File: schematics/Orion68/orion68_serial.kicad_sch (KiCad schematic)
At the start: 32 parts, among them J700 Euro96pin, J701 RS232_1, J702 RS232_1, J703 RS232_1, U18_C? 100nf, U19 74HC138, U20 74HC138, U23 74LS139, U701 UART1, U702 UART2, U703 UART3, Y1 14.745600

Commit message: updating
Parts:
- added U27: 74LS32, symbol 74xx:74LS32
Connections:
- net +5V: no longer U20.6 (E2)
- net A10: no longer U20.3 (A2)
- net A11: now also U27.2; no longer U20.4 (~{E0})
- net A8: no longer U20.1 (A0)
- net A9: no longer U20.2 (A1)
- net /AS: now also U27.5
- net /IO_CS: now also J700.84, U27.12; no longer J700.85, U20.5 (~{E1})
- net /LDS: now also U27.1
- net /UART_CS: now reaches J700.83
- new net: U20.4 (~{E0}), U27.8
- new net: U20.5 (~{E1}), U27.11
- new net: U27.3, U27.9
- new net: U27.10, U27.6
- new net A12: U20.1 (A0)
- new net A13: U20.2 (A1)
- new net A14: U20.3 (A2)
- new net A15: U20.6 (E2)
- new net /IO_CS1: U27.13
- new net /MEM_CS: J700.85
- new net /cpuwr: U27.4
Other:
- note added: "FF9000 – FF9FFF UART0 FF9000 – FF9FFF UART1 FF9900 – FF9FFF UART2 FF9000 – FF9FFF UART3"
- note removed: "FF0100 – FF00FF UART0 FF0200 – FF01FF UART1 FF0300 – FF02FF UART2 FF0400 – FF03FF UART3"
- moved on the sheet: U20

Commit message: B column DIN conn. all in GND
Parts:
- removed J700: Euro96pin, ConnPdSilva:conn_euro96, symbol ConnPdSilva:ConnEuro96
- removed U19: 74HC138, symbol 74xx:74HC138
- removed U23: 74LS139, symbol 74xx:74LS139
- removed U27: 74LS32, symbol 74xx:74LS32
- added J700 (x2): Euro96pin, ConnPdSilva:conn_euro96, symbol ConnPdSilva:ConnEuro96
- added U28: ~, symbol pdSilva:74HC4078
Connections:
- net +12V: now also J700.92, J700.92
- net +5V: now also J700.1, J700.1, J700.33, J700.33, J700.65, J700.65, U28.14 (VCC)
- net -5V: now also J700.94, J700.94
- net A10: now also U20.3 (A2)
- net A11: now also U20.4 (~{E0})
- net A12: now also U28.2 (I1); no longer U20.1 (A0)
- net A13: now also U28.3 (I2); no longer U20.2 (A1)
- net A14: now also U20.6 (E2); no longer U20.3 (A2)
- net A15: now also U28.4 (I3); no longer U20.6 (E2)
- net A8: now also U20.1 (A0)
- net A9: now also U20.2 (A1)
- net ALE: now also J700.73
- net BA0: now also J700.18
- net BA1: now also J700.19, J700.19
- net BA10: now also J700.28, J700.28
- net BA11: now also J700.29, J700.29
- net BA12: now also J700.30, J700.30
- net BA13: now also J700.31, J700.31
- net BA14: now also J700.63, J700.91
- net BA15: now also J700.62, J700.90
- net BA16: now also J700.61, J700.89
- net BA17: now also J700.60, J700.88
- net BA18: now also J700.59, J700.87
- net BA19: now also J700.58, J700.86
- net BA2: now also J700.20, J700.20
- net BA20: now also J700.57, J700.81
- net BA21: now also J700.56, J700.80
- net BA22: now also J700.55, J700.79
- net BA23: now also J700.54, J700.78
- net BA3: now also J700.21, J700.21
- net BA4: now also J700.22, J700.22
- net BA5: now also J700.23, J700.23
- net BA6: now also J700.24, J700.24
- net BA7: now also J700.25, J700.25
- net BA8: now also J700.26, J700.26
- net BA9: now also J700.27, J700.27
- net BD0: now also J700.2, J700.2
- net BD1: now also J700.3, J700.3
- net BD10: now also J700.12, J700.12
- net BD11: now also J700.13, J700.13
- net BD12: now also J700.14, J700.14
- net BD13: now also J700.15, J700.15
- net BD14: now also J700.16, J700.16
- net BD15: now also J700.17, J700.17
- net BD2: now also J700.4, J700.4
- net BD3: now also J700.5, J700.5
- net BD4: now also J700.6, J700.6
- net BD5: now also J700.7, J700.7
- net BD6: now also J700.8, J700.8
- net BD7: now also J700.9, J700.9
- net BD8: now also J700.10, J700.10
- net BD9: now also J700.11, J700.11
- net BOOTIN: now also J700.87
- net B/AS: now also J700.43, J700.69
- net B/LDS: now also J700.70, J700.70
- net B/UDS: now also J700.71, J700.71
- net CPU_CLK: now also J700.81
- net CRUCLK: now also J700.35
- net CRUIN: now also J700.36
- net CRUOUT: now also J700.37
- net DBIN: now also J700.38
- net DT/R: now also J700.75
- net E: now also J700.34
- net GND: now also J700.32, J700.32, J700.64, J700.64, J700.93, J700.93, J700.95, J700.95, J700.96, J700.96
- net GNDREF: now also U28.10 (I6), U28.7 (VCC), U28.9 (I5)
- net HLDA: now also J700.52
- net IAQ: now also J700.39
- net IRQ2: now also J700.48
- net IRQ3: now also J700.49
- net IRQ4: now also J700.50
- net IRQ5: now also J700.89
- net IRQ6: now also J700.90
- net IRQ7: now also J700.91
- net M/IO: now also J700.76
- net NMI: now also J700.41
- net PWR_GOOD: now also J700.88
- net RESET: now also J700.67, J700.67
- net Res9: now also J700.69
- net TICK_IN: now also J700.86
- net /AS: now also U28.5 (I4)
- net /BERR: now also J700.68
- net /CSA: now also U20.15 (~{Y0}); no longer U20.14 (~{Y1})
- net /CSB: now also U20.14 (~{Y1}); no longer U20.13 (~{Y2})
- net /CSC: now also U20.13 (~{Y2}); no longer U20.12 (~{Y3})
- net /CSD: now also U20.12 (~{Y3}); no longer U20.11 (~{Y4})
- net /DEN: now also J700.74
- net /HALT: now also J700.53
- net /HOLD: now also J700.42
- net /INTA: now also J700.72
- net /INTR: now also J700.40
- net /IO_CS: now also J700.84, J700.84, U28.11 (I7)
- net /IO_CS1: now also J700.82, J700.82, U28.12 (I8)
- net /M1: now also J700.79
- net /MEM_CS: now also J700.85, J700.85
- net /RESET: now also J700.66, J700.66
- net /RFSH: now also J700.80
- net /RST: now also J700.51
- net /SSO: now also J700.77
- net /UART_CS: now also J700.83
- net /WAIT: now also J700.78
- net /iord: now also J700.44
- net /iowr: now also J700.47
- net /memrd: now also J700.45
- net /memwr: now also J700.46
- net at U20.5 (~{E1}): now also U28.1 (O1)
- no-connect marks 24 -> 20
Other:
- note added: "1 2 3 4 5 6 7 8 9 10 11 12 13 14 15"
- note added: "15 14 13 12 11 10"
- note added: "15 14 13 12 11 10 9 8 7 6 5 4 3 2 1"
- note added: "23 22 21 20 19 18 17 16 15 14 13 12 11 10 09 08 07 06 05 04 03 02 01 00 1 1 1 1 1 1 1 1 0 1 0 0 0 0 0 0 0 0 0 0 0 0 0 0 F F 4 0 0 0"
- note added: "FF4000 – FF40FF UART0 FF4100 – FF91FF UART1 FF4200 - FF92FF UART2 FF4300 - FF93FF UART3"
- note removed: "FF9000 – FF9FFF UART0 FF9000 – FF9FFF UART1 FF9900 – FF9FFF UART2 FF9000 – FF9FFF UART3"
- note removed: "O que o manual está te dizendo (Tradução para o Orion68K): GINT (Global Interrupt) no Pino INT0: Se você configurar o bit AFR[4] como '1', o chip para de usar vários pinos de interrupção e concentra tudo no pino INT0. Isso é ótimo para economizar trilhas no seu wire-up. Inversão via Software (O melhor de tudo!): O bit AFR[5] é o seu "inversor digital". Se você deixar AFR[5] em '0' (que é o padrão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"
- moved on the sheet: U20

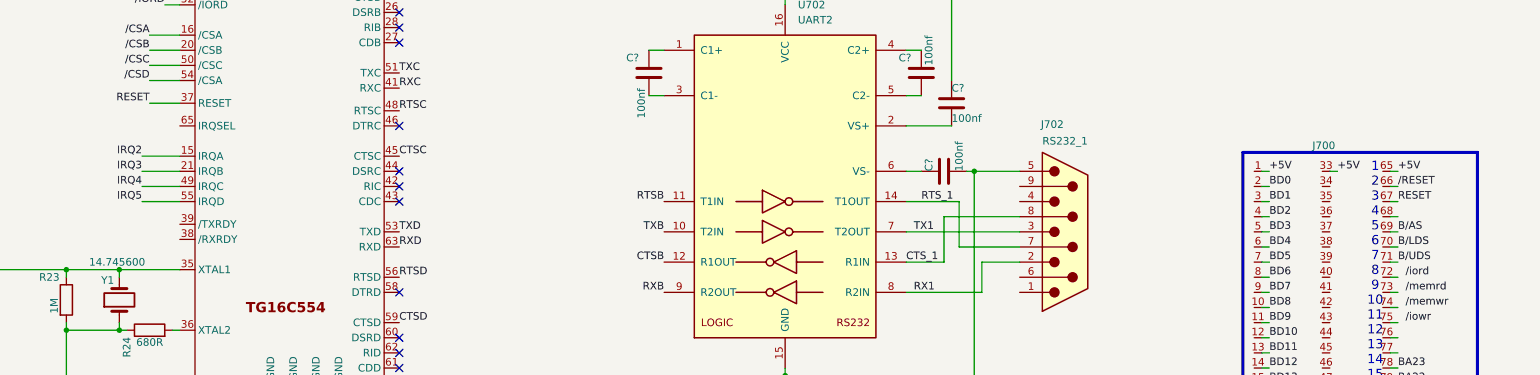
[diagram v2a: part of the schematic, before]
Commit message: Added drv_keboard
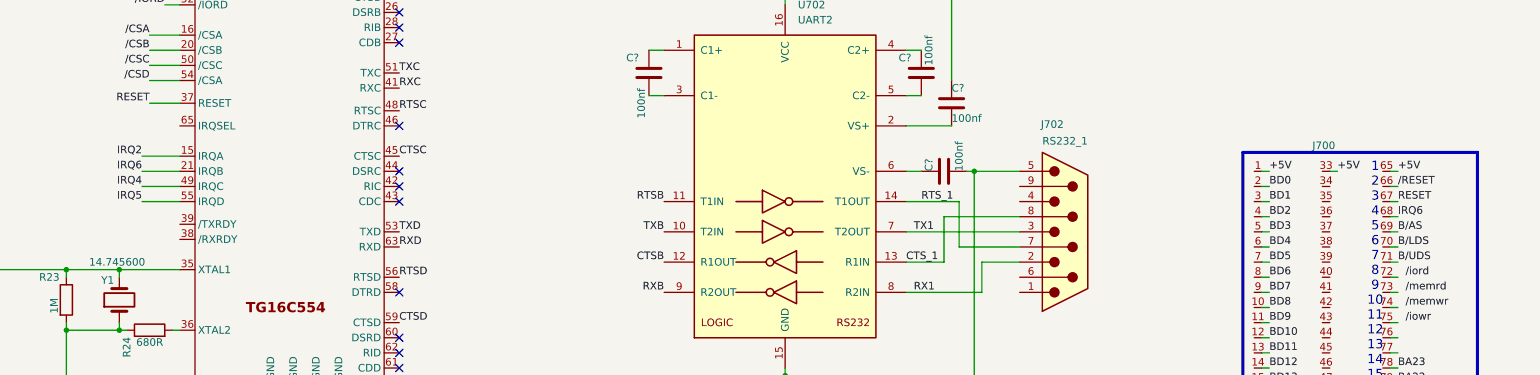
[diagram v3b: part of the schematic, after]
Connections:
- net IRQ3: no longer U700.21 (IRQB)
- net IRQ6: now also J700.68, U700.21 (IRQB)
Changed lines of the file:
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@@
+		)
+	)
+	(label "IRQ6"
+		(at 361.95 142.24 0)
+		(effects
+			(font
+				(size 1.27 1.27)
+			)
+			(justify left bottom)
 		)
 	)
@@
 		)
 	)
-	(label "IRQ3"
+	(label "IRQ6"
 		(at 151.13 134.62 180)
 		(effects
